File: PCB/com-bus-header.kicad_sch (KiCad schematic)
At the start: 6 parts, among them IC6 SN75C3232EPWR

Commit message: re-annotate schematic
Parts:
- renumbered C51 to C56, C52 to C57, C53 to C58, C55 to C60, IC6 to IC8
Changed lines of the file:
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@@
   (symbol (lib_id "SamacSys_Parts:UUP1H0R1MCL1GS") (at 205.105 95.885 180) (unit 1)
     (in_bom yes) (on_board yes) (dnp no)
-    (property "Reference" "C55" (at 203.835 97.155 0)
+    (property "Reference" "C60" (at 203.835 97.155 0)
       (effects (font (size 1.27 1.27)))
     )
@@
       (project "OroLink"
         (path "/e89dcd22-1250-4a5b-b778-1c95a0dd623d/a5104146-06a0-496e-bda0-1e4731a261c3"
-          (reference "C55") (unit 1)
+          (reference "C60") (unit 1)
         )
       )
@@
   (symbol (lib_id "SamacSys_Parts:SN75C3232EPWR") (at 86.36 86.995 0) (unit 1)
     (in_bom yes) (on_board yes) (dnp no)
-    (property "Reference" "IC6" (at 101.6 80.645 0)
+    (property "Reference" "IC8" (at 101.6 80.645 0)
       (effects (font (size 1.27 1.27)))
     )
@@
       (project "OroLink"
         (path "/e89dcd22-1250-4a5b-b778-1c95a0dd623d/a5104146-06a0-496e-bda0-1e4731a261c3"
-          (reference "IC6") (unit 1)
+          (reference "IC8") (unit 1)
         )
       )
@@
   (symbol (lib_id "power:GND") (at 149.225 89.535 0) (unit 1)
     (in_bom yes) (on_board yes) (dnp no) (fields_autoplaced)
-    (property "Reference" "#PWR074" (at 149.225 95.885 0)
+    (property "Reference" "#PWR077" (at 149.225 95.885 0)
       (effects (font (size 1.27 1.27)) hide)
     )
@@
       (project "OroLink"
         (path "/e89dcd22-1250-4a5b-b778-1c95a0dd623d/a5104146-06a0-496e-bda0-1e4731a261c3"
-          (reference "#PWR074") (unit 1)
+          (reference "#PWR077") (unit 1)
         )
       )
@@
   (symbol (lib_id "power:GND") (at 212.725 113.665 0) (unit 1)
     (in_bom yes) (on_board yes) (dnp no) (fields_autoplaced)
-    (property "Reference" "#PWR076" (at 212.725 120.015 0)
+    (property "Reference" "#PWR079" (at 212.725 120.015 0)
       (effects (font (size 1.27 1.27)) hide)
     )
@@
       (project "OroLink"
         (path "/e89dcd22-1250-4a5b-b778-1c95a0dd623d/a5104146-06a0-496e-bda0-1e4731a261c3"
-          (reference "#PWR076") (unit 1)
+          (reference "#PWR079") (unit 1)
         )
       )
@@
   (symbol (lib_id "SamacSys_Parts:UUP1H0R1MCL1GS") (at 192.405 102.235 0) (unit 1)
     (in_bom yes) (on_board yes) (dnp no)
-    (property "Reference" "C53" (at 203.835 103.505 0)
+    (property "Reference" "C58" (at 203.835 103.505 0)
       (effects (font (size 1.27 1.27)))
     )
@@
       (project "OroLink"
         (path "/e89dcd22-1250-4a5b-b778-1c95a0dd623d/a5104146-06a0-496e-bda0-1e4731a261c3"
-          (reference "C53") (unit 1)
+          (reference "C58") (unit 1)
         )
       )
@@
   (symbol (lib_id "power:+3V3") (at 119.38 86.995 0) (unit 1)
     (in_bom yes) (on_board yes) (dnp no) (fields_autoplaced)
-    (property "Reference" "#PWR073" (at 119.38 90.805 0)
+    (property "Reference" "#PWR076" (at 119.38 90.805 0)
       (effects (font (size 1.27 1.27)) hide)
     )
@@
       (project "OroLink"
         (path "/e89dcd22-1250-4a5b-b778-1c95a0dd623d/a5104146-06a0-496e-bda0-1e4731a261c3"
-          (reference "#PWR073") (unit 1)
+          (reference "#PWR076") (unit 1)
         )
       )
@@
         )
         (path "/e89dcd22-1250-4a5b-b778-1c95a0dd623d/a5104146-06a0-496e-bda0-1e4731a261c3"
-          (reference "C54") (unit 1)
+          (reference "C59") (unit 1)
         )
       )
@@
   (symbol (lib_id "power:+3V3") (at 184.785 108.585 0) (unit 1)
     (in_bom yes) (on_board yes) (dnp no) (fields_autoplaced)
-    (property "Reference" "#PWR075" (at 184.785 112.395 0)
+    (property "Reference" "#PWR078" (at 184.785 112.395 0)
       (effects (font (size 1.27 1.27)) hide)
     )
@@
       (project "OroLink"
         (path "/e89dcd22-1250-4a5b-b778-1c95a0dd623d/a5104146-06a0-496e-bda0-1e4731a261c3"
-          (reference "#PWR075") (unit 1)
+          (reference "#PWR078") (unit 1)
         )
       )
@@
   (symbol (lib_id "SamacSys_Parts:UUP1H0R1MCL1GS") (at 192.405 83.185 0) (unit 1)
     (in_bom yes) (on_board yes) (dnp no)
-    (property "Reference" "C51" (at 203.835 84.455 0)
+    (property "Reference" "C56" (at 203.835 84.455 0)
       (effects (font (size 1.27 1.27)))
     )
@@
       (project "OroLink"
         (path "/e89dcd22-1250-4a5b-b778-1c95a0dd623d/a5104146-06a0-496e-bda0-1e4731a261c3"
-          (reference "C51") (unit 1)
+          (reference "C56") (unit 1)
         )
       )
@@
   (symbol (lib_id "SamacSys_Parts:UUP1H0R1MCL1GS") (at 192.405 89.535 0) (unit 1)
     (in_bom yes) (on_board yes) (dnp no)
-    (property "Reference" "C52" (at 203.835 90.805 0)
+    (property "Reference" "C57" (at 203.835 90.805 0)
       (effects (font (size 1.27 1.27)))
     )
@@
       (project "OroLink"
         (path "/e89dcd22-1250-4a5b-b778-1c95a0dd623d/a5104146-06a0-496e-bda0-1e4731a261c3"
-          (reference "C52") (unit 1)
-        )
-      )
+          (reference "C57") (unit 1)
+        )
+      )

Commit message: replace 0.1u caps with larger package (closes #2)
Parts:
- C16: footprint SamacSys_Parts:CAPC0402X22N -> CAPC1005X33N; symbol SamacSys_Parts:GRT31C5C1H104FA02L -> SamacSys_Parts:MSAST1L3YB5104KFNA01; Arrow Part Number 01016D104KAT2A -> (none); Arrow Price/Stock https://www.arrow.com/en/products/01016d104kat2a/avx -> (none); Height 0.22 -> 0.33; Manufacturer_Name AVX -> TAIYO YUDEN; Manufacturer_Part_Number 01016D104KAT2A -> MSAST1L3YB5104KFNA01; Mouser Part Number 581-01016D104KAT2A -> (none); Mouser Price/Stock https://www.mouser.com/Search/Refine.aspx?Keyword=581-01016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 -> (none)
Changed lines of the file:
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@@
     )
   )
-  (symbol (lib_id "SamacSys_Parts:GRT31C5C1H104FA02L") (at 192.405 108.585 0) (mirror x) (unit 1)
+  (symbol (lib_id "SamacSys_Parts:MSAST1L3YB5104KFNA01") (at 192.405 108.585 0) (mirror x) (unit 1)
     (in_bom yes) (on_board yes) (dnp no)
     (property "Reference" "C16" (at 203.835 110.49 0)
@@
       (effects (font (size 1.27 1.27)) hide)
     )
-    (property "Footprint" "SamacSys_Parts:CAPC0402X22N" (at 201.295 109.855 0)
+    (property "Footprint" "CAPC1005X33N" (at 201.295 109.855 0)
       (effects (font (size 1.27 1.27)) (justify left) hide)
     )
-    (property "Datasheet" "https://altium.componentsearchengine.com/Datasheets/1/01016D104KAT2A.pdf" (at 201.295 107.315 0)
+    (property "Datasheet" "https://www.mouser.de/datasheet/2/396/TaiyoYuden_MSAST1L3YB5104KFNA01_SS-3009733.pdf" (at 201.295 107.315 0)
       (effects (font (size 1.27 1.27)) (justify left) hide)
     )
-    (property "Description" "Multilayer Ceramic Capacitors MLCC - SMD/SMT 6.3V .1uF X5R 0101 10%" (at 201.295 104.775 0)
+    (property "Description" "Multilayer Ceramic Capacitors MLCC - SMD/SMT 0402 25VDC 0.1uF 10% X5R" (at 201.295 104.775 0)
       (effects (font (size 1.27 1.27)) (justify left) hide)
     )
-    (property "Height" "0.22" (at 201.295 102.235 0)
+    (property "Height" "0.33" (at 201.295 102.235 0)
       (effects (font (size 1.27 1.27)) (justify left) hide)
     )
-    (property "Manufacturer_Name" "AVX" (at 201.295 99.695 0)
+    (property "Manufacturer_Name" "TAIYO YUDEN" (at 201.295 99.695 0)
       (effects (font (size 1.27 1.27)) (justify left) hide)
     )
-    (property "Manufacturer_Part_Number" "01016D104KAT2A" (at 201.295 97.155 0)
+    (property "Manufacturer_Part_Number" "MSAST1L3YB5104KFNA01" (at 201.295 97.155 0)
       (effects (font (size 1.27 1.27)) (justify left) hide)
     )
-    (property "Mouser Part Number" "581-01016D104KAT2A" (at 201.295 94.615 0)
+    (property "Mouser Part Number" "" (at 201.295 94.615 0)
       (effects (font (size 1.27 1.27)) (justify left) hide)
     )
-    (property "Mouser Price/Stock" "https://www.mouser.com/Search/Refine.aspx?Keyword=581-01016D104KAT2A" (at 201.295 92.075 0)
+    (property "Mouser Price/Stock" "" (at 201.295 92.075 0)
       (effects (font (size 1.27 1.27)) (justify left) hide)
     )
-    (property "Arrow Part Number" "01016D104KAT2A" (at 201.295 89.535 0)
+    (property "Arrow Part Number" "" (at 201.295 89.535 0)
       (effects (font (size 1.27 1.27)) (justify left) hide)
     )
-    (property "Arrow Price/Stock" "https://www.arrow.com/en/products/01016d104kat2a/avx" (at 201.295 86.995 0)
+    (property "Arrow Price/Stock" "" (at 201.295 86.995 0)
       (effects (font (size 1.27 1.27)) (justify left) hide)
     )

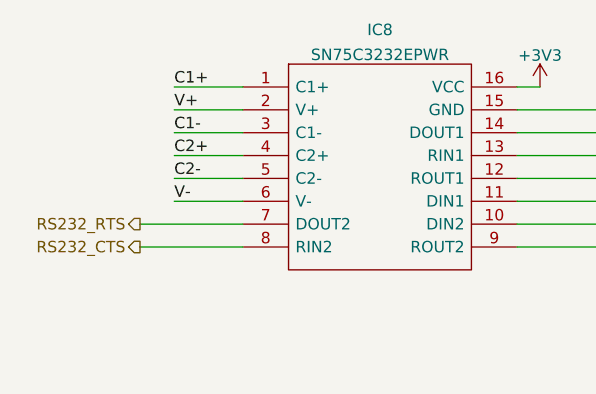
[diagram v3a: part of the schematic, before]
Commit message: add debug pins to signal lines (closes #16)
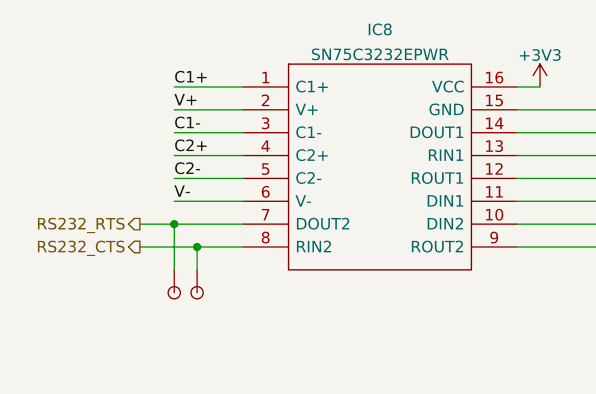
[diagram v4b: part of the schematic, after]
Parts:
- added DBG5 (x2): ~, Oro Footprints:DebugPin, symbol Oro:DebugPin
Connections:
- net RS232_CTS: now also DBG5.1
- net RS232_RTS: now also DBG5.1
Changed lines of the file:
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@@
     (comment 2 "Joshua Lee Junon")
   )
+  (junction (at 78.74 102.235) (diameter 0) (color 0 0 0 0)
+  )
   (junction (at 212.725 102.235) (diameter 0) (color 0 0 0 0)
   )
   (junction (at 212.725 108.585) (diameter 0) (color 0 0 0 0)
   )
+  (junction (at 81.28 104.775) (diameter 0) (color 0 0 0 0)
+  )
   (wire (pts (xy 116.84 92.075) (xy 128.27 92.075))
     (stroke (width 0) (type default))
   )
+  (wire (pts (xy 78.74 102.235) (xy 78.74 107.315))
+    (stroke (width 0) (type default))
+  )
   (wire (pts (xy 212.725 108.585) (xy 212.725 113.665))
     (stroke (width 0) (type default))
@@
     (stroke (width 0) (type default))
   )
+  (wire (pts (xy 78.74 102.235) (xy 74.93 102.235))
+    (stroke (width 0) (type default))
+  )
   (wire (pts (xy 78.74 89.535) (xy 86.36 89.535))
     (stroke (width 0) (type default))
@@
     (stroke (width 0) (type default))
   )
+  (wire (pts (xy 81.28 104.775) (xy 86.36 104.775))
+    (stroke (width 0) (type default))
+  )
   (wire (pts (xy 212.725 83.185) (xy 205.105 83.185))
     (stroke (width 0) (type default))
@@
     (stroke (width 0) (type default))
   )
-  (wire (pts (xy 74.93 104.775) (xy 86.36 104.775))
+  (wire (pts (xy 74.93 104.775) (xy 81.28 104.775))
     (stroke (width 0) (type default))
   )
@@
     (stroke (width 0) (type default))
   )
-  (wire (pts (xy 86.36 102.235) (xy 74.93 102.235))
+  (wire (pts (xy 86.36 102.235) (xy 78.74 102.235))
+    (stroke (width 0) (type default))
+  )
+  (wire (pts (xy 81.28 104.775) (xy 81.28 107.315))
     (stroke (width 0) (type default))
   )
@@
     )
   )
+  (symbol (lib_id "Oro:DebugPin") (at 78.74 107.315 270) (unit 1)
+    (in_bom no) (on_board yes) (dnp no)
+    (property "Reference" "DBG5" (at 78.74 113.03 0)
+      (effects (font (size 1.27 1.27)) hide)
+    )
+    (property "Value" "~" (at 78.74 107.315 0)
+      (effects (font (size 1.27 1.27)) hide)
+    )
+    (property "Footprint" "Oro Footprints:DebugPin" (at 81.28 108.585 0)
+      (effects (font (size 1.27 1.27)) hide)
+    )
+    (property "Datasheet" "" (at 78.74 107.315 0)
+      (effects (font (size 1.27 1.27)) hide)
+    )
+    (property "Sim.Enable" "0" (at 81.28 121.285 0)
+      (effects (font (size 1.27 1.27)) hide)
+    )
+    (pin "1")
+    (instances
+      (project "OroLink"
+        (path "/e89dcd22-1250-4a5b-b778-1c95a0dd623d/f955395e-bf1a-4ef3-9cfe-ec9d49f66988"
+          (reference "DBG5") (unit 1)
+        )
+        (path "/e89dcd22-1250-4a5b-b778-1c95a0dd623d/1b3eede1-74b0-4c0b-b4f1-7ec1bfc1f54f"
+          (reference "DBG16") (unit 1)
+        )
+        (path "/e89dcd22-1250-4a5b-b778-1c95a0dd623d/52771c01-2e58-4900-abe5-411f688d020f"
+          (reference "DBG25") (unit 1)
+        )
+        (path "/e89dcd22-1250-4a5b-b778-1c95a0dd623d/7cebe953-3148-4b67-a6c9-1f2594261687"
+          (reference "DBG26") (unit 1)
+        )
+        (path "/e89dcd22-1250-4a5b-b778-1c95a0dd623d/a5104146-06a0-496e-bda0-1e4731a261c3"
+          (reference "DBG29") (unit 1)
+        )
+      )
+    )
+  )
   (symbol (lib_id "power:GND") (at 149.225 89.535 0) (unit 1)
     (in_bom yes) (on_board yes) (dnp no) (fields_autoplaced)
@@
         )
       )
+    )
+  )
+  (symbol (lib_id "Oro:DebugPin") (at 81.28 107.315 270) (unit 1)
+    (in_bom no) (on_board yes) (dnp no)
+    (property "Reference" "DBG5" (at 81.28 113.03 0)
+      (effects (font (size 1.27 1.27)) hide)
+    )
+    (property "Value" "~" (at 81.28 107.315 0)
+      (effects (font (size 1.27 1.27)) hide)
+    )
+    (property "Footprint" "Oro Footprints:DebugPin" (at 83.82 108.585 0)
+      (effects (font (size 1.27 1.27)) hide)
+    )
+    (property "Datasheet" "" (at 81.28 107.315 0)
+      (effects (font (size 1.27 1.27)) hide)
+    )
+    (property "Sim.Enable" "0" (at 83.82 121.285 0)
+      (effects (font (size 1.27 1.27)) hide)
+    )
+    (pin "1")
+    (instances
+      (project "OroLink"
+        (path "/e89dcd22-1250-4a5b-b778-1c95a0dd623d/f955395e-bf1a-4ef3-9cfe-ec9d49f66988"
+          (reference "DBG5") (unit 1)
+        )
+        (path "/e89dcd22-1250-4a5b-b778-1c95a0dd623d/1b3eede1-74b0-4c0b-b4f1-7ec1bfc1f54f"
+          (reference "DBG16") (unit 1)
+        )
+        (path "/e89dcd22-1250-4a5b-b778-1c95a0dd623d/52771c01-2e58-4900-abe5-411f688d020f"
+          (reference "DBG25") (unit 1)
+        )
+        (path "/e89dcd22-1250-4a5b-b778-1c95a0dd623d/7cebe953-3148-4b67-a6c9-1f2594261687"
+          (reference "DBG26") (unit 1)
+        )
+        (path "/e89dcd22-1250-4a5b-b778-1c95a0dd623d/a5104146-06a0-496e-bda0-1e4731a261c3"
+          (reference "DBG30") (unit 1)
+        )
+      )

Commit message: preliminary routing completed
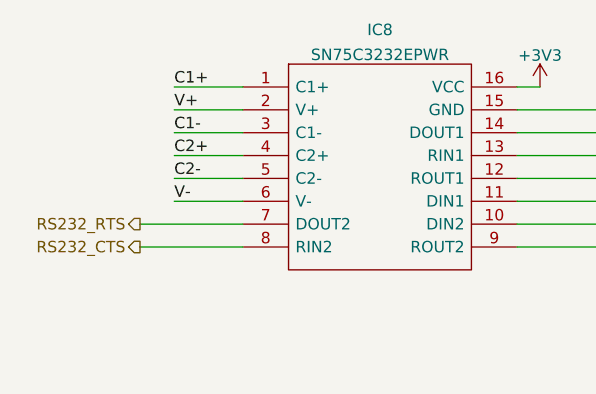
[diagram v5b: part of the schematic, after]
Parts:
- removed DBG5 (x2): ~, Oro Footprints:DebugPin, symbol Oro:DebugPin
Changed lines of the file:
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@@
     (comment 2 "Joshua Lee Junon")
   )
-  (junction (at 78.74 102.235) (diameter 0) (color 0 0 0 0)
-  )
   (junction (at 212.725 102.235) (diameter 0) (color 0 0 0 0)
   )
   (junction (at 212.725 108.585) (diameter 0) (color 0 0 0 0)
   )
-  (junction (at 81.28 104.775) (diameter 0) (color 0 0 0 0)
-  )
   (wire (pts (xy 116.84 92.075) (xy 128.27 92.075))
     (stroke (width 0) (type default))
   )
-  (wire (pts (xy 78.74 102.235) (xy 78.74 107.315))
-    (stroke (width 0) (type default))
-  )
   (wire (pts (xy 212.725 108.585) (xy 212.725 113.665))
     (stroke (width 0) (type default))
@@
     (stroke (width 0) (type default))
   )
-  (wire (pts (xy 78.74 102.235) (xy 74.93 102.235))
-    (stroke (width 0) (type default))
-  )
   (wire (pts (xy 78.74 89.535) (xy 86.36 89.535))
     (stroke (width 0) (type default))
@@
     (stroke (width 0) (type default))
   )
-  (wire (pts (xy 81.28 104.775) (xy 86.36 104.775))
-    (stroke (width 0) (type default))
-  )
   (wire (pts (xy 212.725 83.185) (xy 205.105 83.185))
     (stroke (width 0) (type default))
@@
     (stroke (width 0) (type default))
   )
-  (wire (pts (xy 74.93 104.775) (xy 81.28 104.775))
+  (wire (pts (xy 74.93 104.775) (xy 86.36 104.775))
     (stroke (width 0) (type default))
   )
@@
     (stroke (width 0) (type default))
   )
-  (wire (pts (xy 86.36 102.235) (xy 78.74 102.235))
-    (stroke (width 0) (type default))
-  )
-  (wire (pts (xy 81.28 104.775) (xy 81.28 107.315))
+  (wire (pts (xy 74.93 102.235) (xy 86.36 102.235))
     (stroke (width 0) (type default))
   )
@@
     )
   )
-  (symbol (lib_id "Oro:DebugPin") (at 78.74 107.315 270) (unit 1)
-    (in_bom no) (on_board yes) (dnp no)
-    (property "Reference" "DBG5" (at 78.74 113.03 0)
-      (effects (font (size 1.27 1.27)) hide)
-    )
-    (property "Value" "~" (at 78.74 107.315 0)
-      (effects (font (size 1.27 1.27)) hide)
-    )
-    (property "Footprint" "Oro Footprints:DebugPin" (at 81.28 108.585 0)
-      (effects (font (size 1.27 1.27)) hide)
-    )
-    (property "Datasheet" "" (at 78.74 107.315 0)
-      (effects (font (size 1.27 1.27)) hide)
-    )
-    (property "Sim.Enable" "0" (at 81.28 121.285 0)
-      (effects (font (size 1.27 1.27)) hide)
-    )
-    (pin "1")
-    (instances
-      (project "OroLink"
-        (path "/e89dcd22-1250-4a5b-b778-1c95a0dd623d/f955395e-bf1a-4ef3-9cfe-ec9d49f66988"
-          (reference "DBG5") (unit 1)
-        )
-        (path "/e89dcd22-1250-4a5b-b778-1c95a0dd623d/1b3eede1-74b0-4c0b-b4f1-7ec1bfc1f54f"
-          (reference "DBG16") (unit 1)
-        )
-        (path "/e89dcd22-1250-4a5b-b778-1c95a0dd623d/52771c01-2e58-4900-abe5-411f688d020f"
-          (reference "DBG25") (unit 1)
-        )
-        (path "/e89dcd22-1250-4a5b-b778-1c95a0dd623d/7cebe953-3148-4b67-a6c9-1f2594261687"
-          (reference "DBG26") (unit 1)
-        )
-        (path "/e89dcd22-1250-4a5b-b778-1c95a0dd623d/a5104146-06a0-496e-bda0-1e4731a261c3"
-          (reference "DBG29") (unit 1)
-        )
-      )
-    )
-  )
   (symbol (lib_id "power:GND") (at 149.225 89.535 0) (unit 1)
     (in_bom yes) (on_board yes) (dnp no) (fields_autoplaced)
@@
         )
       )
-    )
-  )
-  (symbol (lib_id "Oro:DebugPin") (at 81.28 107.315 270) (unit 1)
-    (in_bom no) (on_board yes) (dnp no)
-    (property "Reference" "DBG5" (at 81.28 113.03 0)
-      (effects (font (size 1.27 1.27)) hide)
-    )
-    (property "Value" "~" (at 81.28 107.315 0)
-      (effects (font (size 1.27 1.27)) hide)
-    )
-    (property "Footprint" "Oro Footprints:DebugPin" (at 83.82 108.585 0)
-      (effects (font (size 1.27 1.27)) hide)
-    )
-    (property "Datasheet" "" (at 81.28 107.315 0)
-      (effects (font (size 1.27 1.27)) hide)
-    )
-    (property "Sim.Enable" "0" (at 83.82 121.285 0)
-      (effects (font (size 1.27 1.27)) hide)
-    )
-    (pin "1")
-    (instances
-      (project "OroLink"
-        (path "/e89dcd22-1250-4a5b-b778-1c95a0dd623d/f955395e-bf1a-4ef3-9cfe-ec9d49f66988"
-          (reference "DBG5") (unit 1)
-        )
-        (path "/e89dcd22-1250-4a5b-b778-1c95a0dd623d/1b3eede1-74b0-4c0b-b4f1-7ec1bfc1f54f"
-          (reference "DBG16") (unit 1)
-        )
-        (path "/e89dcd22-1250-4a5b-b778-1c95a0dd623d/52771c01-2e58-4900-abe5-411f688d020f"
-          (reference "DBG25") (unit 1)
-        )
-        (path "/e89dcd22-1250-4a5b-b778-1c95a0dd623d/7cebe953-3148-4b67-a6c9-1f2594261687"
-          (reference "DBG26") (unit 1)
-        )
-        (path "/e89dcd22-1250-4a5b-b778-1c95a0dd623d/a5104146-06a0-496e-bda0-1e4731a261c3"
-          (reference "DBG30") (unit 1)
-        )
-      )
